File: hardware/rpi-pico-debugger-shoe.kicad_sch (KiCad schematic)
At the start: 61 parts, among them J12 Conn_01x02_Female, J13 Conn_01x05_Female, J14 USB_C_Receptacle_USB2.0, J15 Conn_01x02_Female, J2 Conn_01x02, J3 Conn_01x03, J4 Conn_01x02_Female, J5 Conn_01x02_Female, J6 KPJX-4S-S, J9 Conn_01x02_Female, SW1 PTS810_SJK_250_SMTR_LFS, U1 RP2040, U2 HT75xx-1-SOT89, U3 W25Q16JVSSIQ, Y1 Crystal_GND2

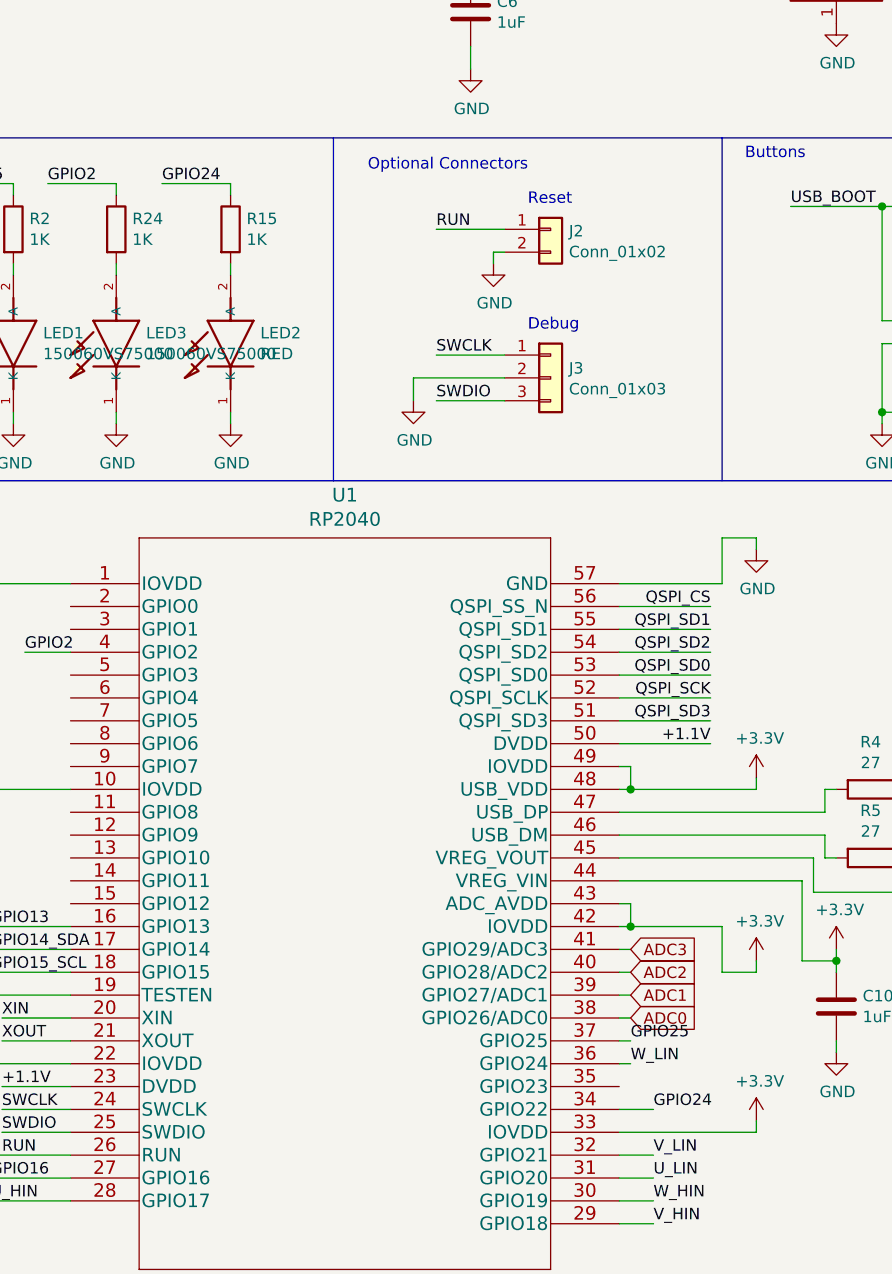
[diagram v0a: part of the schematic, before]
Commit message: updated led gpio
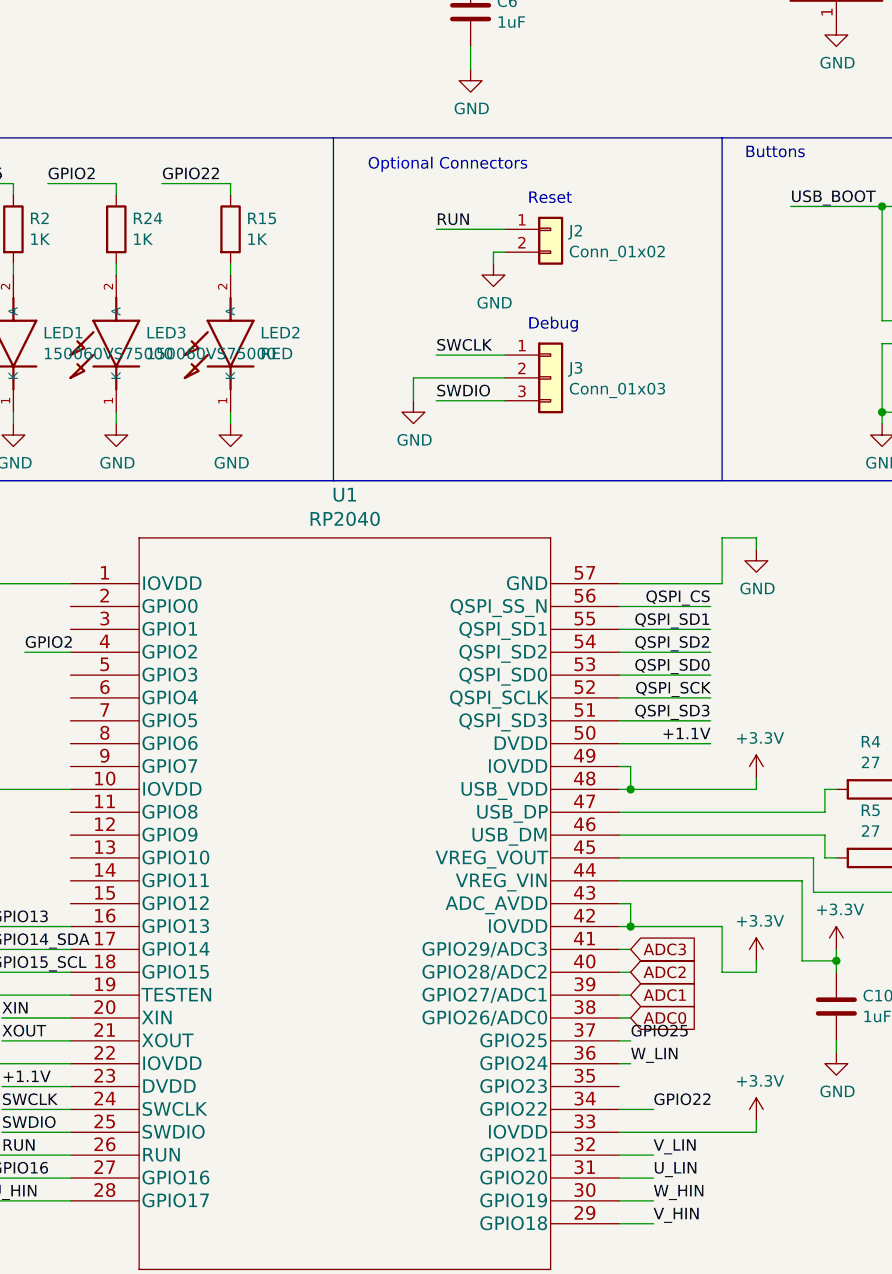
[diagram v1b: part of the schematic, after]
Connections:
- net GPIO24 renamed GPIO22
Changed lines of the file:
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@@
     (effects (font (size 1.27 1.27)) (justify right bottom))
   )
-  (label "GPIO24" (at 99.06 153.67 0) (fields_autoplaced)
+  (label "GPIO22" (at 99.06 153.67 0) (fields_autoplaced)
     (effects (font (size 1.27 1.27)) (justify left bottom))
   )
@@
     (effects (font (size 1.27 1.27)) (justify left bottom))
   )
-  (label "GPIO24" (at 44.45 50.8 0) (fields_autoplaced)
+  (label "GPIO22" (at 44.45 50.8 0) (fields_autoplaced)
     (effects (font (size 1.27 1.27)) (justify left bottom))
   )
